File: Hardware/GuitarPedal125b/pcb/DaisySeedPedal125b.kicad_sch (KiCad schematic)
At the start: 8 parts, among them J1 Barrel_Jack_Switch, J2 AUDIO_IN_TRS, J3 MIDI IN JACK, J4 AUDIO_OUT_TRS, J5 MIDI OUT JACK, J6 Conn_01x20_Socket, J7 Conn_01x20_Socket

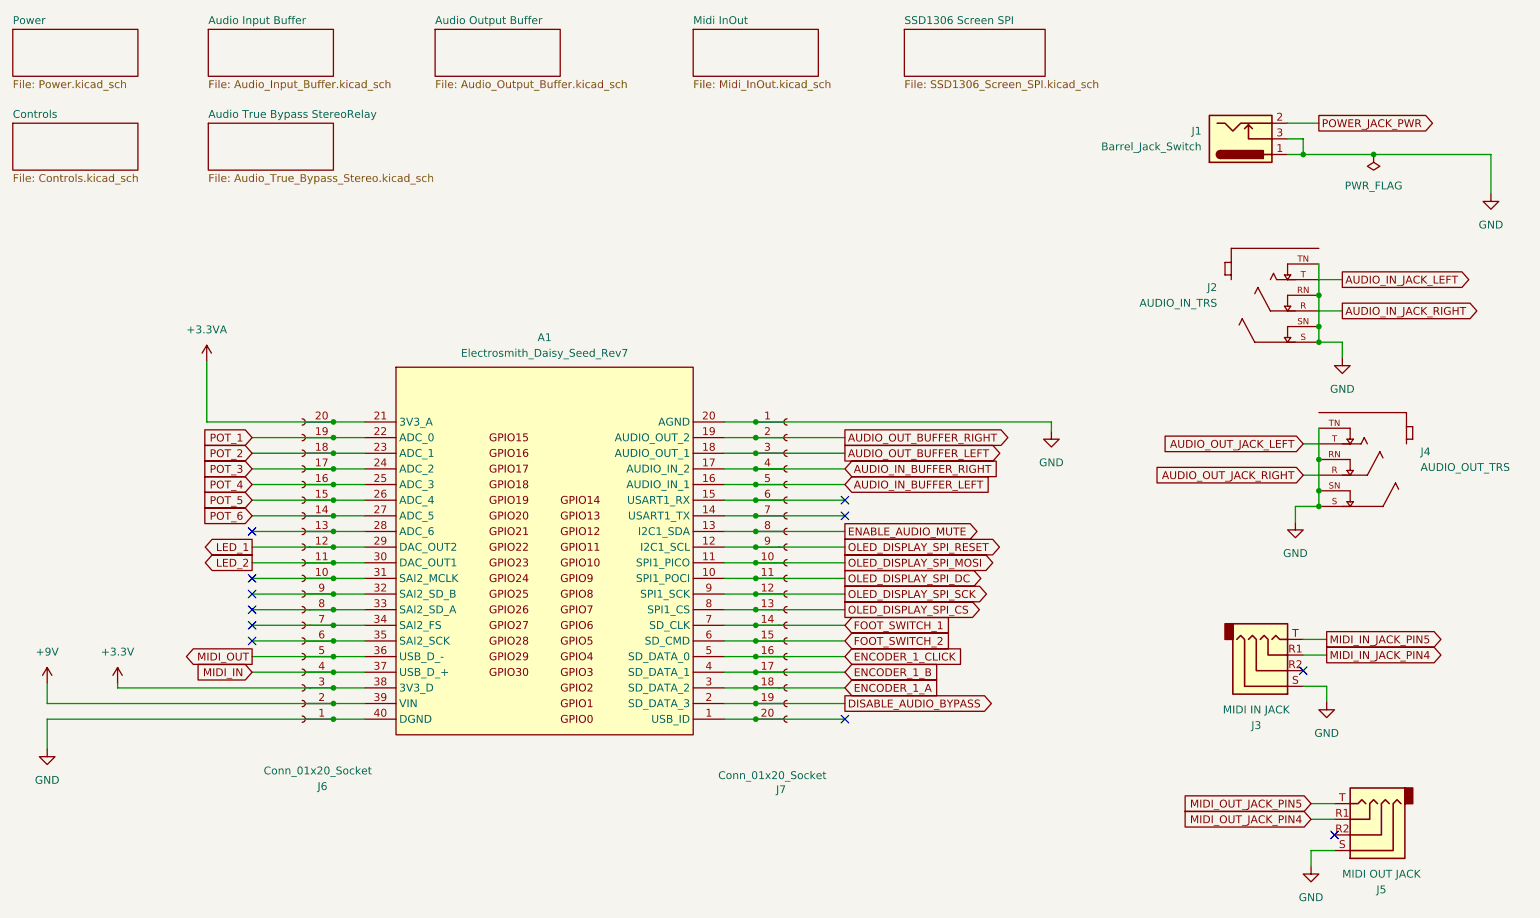
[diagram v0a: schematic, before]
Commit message: Replace screen and encoder by 3 toggle switches and SD card reader.
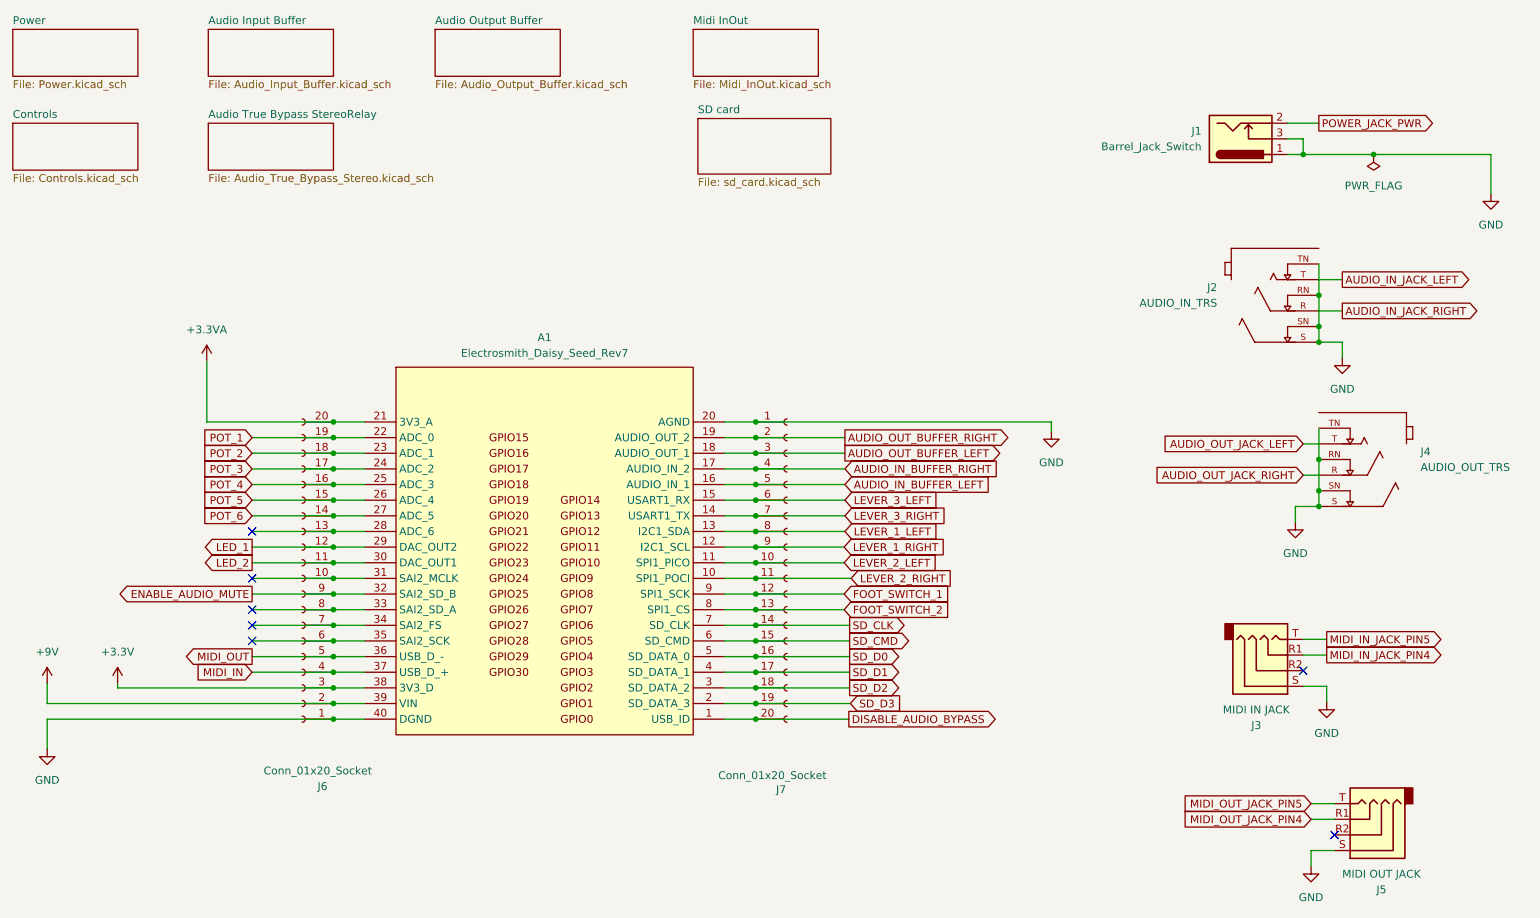
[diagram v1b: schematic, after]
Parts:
- J1: MPN (none) -> C136744; now left out of the parts list
- J2, J4: footprint NMJ6HCD2:NEUTRIK_NMJ6HCD2 -> Connector_Audio:Jack_6.35mm_Neutrik_NMJ6HCD2_Horizontal; MPN (none) -> C368502; now left out of the parts list
- J3, J5: MPN (none) -> C2884926; now left out of the parts list
- J6, J7: now left out of the parts list
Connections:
- net OLED_DISPLAY_SPI_CS is gone; now on net FOOT_SWITCH_2: A1.8 (SPI1_CS), J7.13 (Pin_13)
- net OLED_DISPLAY_SPI_SCK is gone; now on net FOOT_SWITCH_1: A1.9 (SPI1_SCK), J7.12 (Pin_12)
- net DISABLE_AUDIO_BYPASS: now also A1.1 (USB_ID), J7.20 (Pin_20); no longer A1.2 (SD_DATA_3), J7.19 (Pin_19)
- net ENABLE_AUDIO_MUTE: now also A1.32 (SAI2_SD_B), J6.9 (Pin_9); no longer A1.13 (I2C1_SDA), J7.8 (Pin_8)
- net FOOT_SWITCH_1: no longer A1.7 (SD_CLK), J7.14 (Pin_14)
- net FOOT_SWITCH_2: no longer A1.6 (SD_CMD), J7.15 (Pin_15)
- net LEVER_3_LEFT: now reaches A1.15 (USART1_RX), J7.6 (Pin_6)
- net LEVER_3_RIGHT: now reaches A1.14 (USART1_TX), J7.7 (Pin_7)
- net ENCODER_1_A renamed SD_D2
- net ENCODER_1_B renamed SD_D1
- net ENCODER_1_CLICK renamed SD_D0
- net OLED_DISPLAY_SPI_DC renamed LEVER_2_RIGHT
- net OLED_DISPLAY_SPI_MOSI renamed LEVER_2_LEFT
- net OLED_DISPLAY_SPI_RESET renamed LEVER_1_RIGHT
- new net LEVER_1_LEFT: A1.13 (I2C1_SDA), J7.8 (Pin_8)
- new net SD_CLK: A1.7 (SD_CLK), J7.14 (Pin_14)
- new net SD_CMD: A1.6 (SD_CMD), J7.15 (Pin_15)
- new net SD_D3: A1.2 (SD_DATA_3), J7.19 (Pin_19)
- no-connect marks 11 -> 7
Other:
- removed sheet SSD1306 Screen SPI
- added sheet SD card (sd_card.kicad_sch)
